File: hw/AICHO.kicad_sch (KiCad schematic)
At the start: 31 parts, among them J1 Conn_01x06, J2 Conn_01x02, J3 USB_A, U1 RP2040, U2 W25Q128JVPIQ, U3 SPX3819M5-L-3-3, Y1 12MHz

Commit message: Finish board schematic
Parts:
- added C18: 10u, Capacitor_SMD:C_0603_1608Metric, symbol Device:C
- added C19: 100n, Capacitor_SMD:C_0603_1608Metric, symbol Device:C
- added J101, J201, J301, J401: Conn_01x03, Connector_PinHeader_2.54mm:PinHeader_1x03_P2.54mm_Vertical, symbol Connector_Generic:Conn_01x03
- added J102, J103, J104, J202, J203, J204, J302, J303, J304, J402, J403, J404: Conn_01x02, Connector_PinHeader_2.54mm:PinHeader_1x02_P2.54mm_Vertical, symbol Connector_Generic:Conn_01x02
- added J4: AudioJack3_SwitchTR, Connector_Audio:Jack_3.5mm_CUI_SJ1-3525N_Horizontal, symbol Connector_Audio:AudioJack3_SwitchTR
- added J5: Speaker, Connector_PinHeader_2.54mm:PinHeader_1x02_P2.54mm_Vertical, symbol Device:Speaker
- added Q1, Q10, Q11, Q12, Q2, Q3, Q4, Q5, Q6, Q7, Q8, Q9: Si2302, Package_TO_SOT_SMD:SOT-23, symbol Device:Q_NMOS_GSD
- added U4: USBLC6-2SC6, Package_TO_SOT_SMD:SOT-23-6, symbol Power_Protection:USBLC6-2SC6
- added U5: MAX98357AETE+, MAX98357AETE+:QFN50P300X300X80-17N, symbol MAX98357AETE+:MAX98357AETE+
- C1, C10, C11, C12, C13, C14, C15, C2, C3, C4, C5, C6, C7, C8, C9: footprint (none) -> Capacitor_SMD:C_0603_1608Metric
- J1: footprint (none) -> AICHO_footprints:TestPoints_1x06_P2.0
- J2: footprint (none) -> Connector_PinHeader_2.54mm:PinHeader_1x02_P2.54mm_Vertical
- J3: footprint (none) -> Connector_USB:USB_A_CNCTech_1001-011-01101_Horizontal
- JP1: footprint (none) -> Jumper:SolderJumper-2_P1.3mm_Open_RoundedPad1.0x1.5mm
- L1: footprint (none) -> Inductor_SMD:L_0805_2012Metric
- R1, R2, R3, R4, R5: footprint (none) -> Resistor_SMD:R_0603_1608Metric
- Y1: footprint (none) -> Crystal:Crystal_SMD_3225-4Pin_3.2x2.5mm
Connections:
- net +5V: now also C18.1, C19.1, J101.1 (Pin_1), J102.1 (Pin_1), J103.1 (Pin_1), J104.1 (Pin_1), J201.1 (Pin_1), J202.1 (Pin_1), J203.1 (Pin_1), J204.1 (Pin_1), J301.1 (Pin_1), J302.1 (Pin_1), J303.1 (Pin_1), J304.1 (Pin_1), J401.1 (Pin_1), J402.1 (Pin_1), J403.1 (Pin_1), J404.1 (Pin_1), U4.5 (VBUS), U5.4 (~{SD_MODE}), U5.7 (VDD_1), U5.8 (VDD_2)
- net GND: now also J101.3 (Pin_3), J201.3 (Pin_3), J301.3 (Pin_3), J401.3 (Pin_3), Q1.2 (S), Q10.2 (S), Q11.2 (S), Q12.2 (S), Q2.2 (S), Q3.2 (S), Q4.2 (S), Q5.2 (S), Q6.2 (S), Q7.2 (S), Q8.2 (S), Q9.2 (S), U4.2 (GND), U5.11 (GND_2), U5.15 (GND_3), U5.17 (GND_4), U5.3 (GND_1)
- net USB_D+: now also U4.1 (I/O1); no longer J3.3 (D+)
- net USB_D-: now also U4.3 (I/O2); no longer J3.2 (D-)
- net ORG1_LED: now reaches U1.11 (GPIO8)
- net ORG1_LED: now also J101.2 (Pin_2)
- net ORG1_SOLENOID: now reaches U1.12 (GPIO9)
- net ORG1_SOLENOID: now also Q1.1 (G)
- net ORG1_PUMP_INFLATE: now reaches U1.13 (GPIO10)
- net ORG1_PUMP_INFLATE: now also Q2.1 (G)
- net ORG1_PUMP_DRAIN: now reaches U1.14 (GPIO11)
- net ORG1_PUMP_DRAIN: now also Q3.1 (G)
- net ORG2_LED: now reaches U1.15 (GPIO12)
- net ORG2_LED: now also J201.2 (Pin_2)
- net ORG2_SOLENOID: now reaches U1.16 (GPIO13)
- net ORG2_SOLENOID: now also Q4.1 (G)
- net ORG2_PUMP_INFLATE: now reaches U1.17 (GPIO14)
- net ORG2_PUMP_INFLATE: now also Q5.1 (G)
- net ORG2_PUMP_DRAIN: now reaches U1.18 (GPIO15)
- net ORG2_PUMP_DRAIN: now also Q6.1 (G)
- net ORG3_LED: now reaches U1.29 (GPIO18)
- net ORG3_LED: now also J301.2 (Pin_2)
- net ORG3_SOLENOID: now reaches U1.30 (GPIO19)
- net ORG3_SOLENOID: now also Q7.1 (G)
- net ORG3_PUMP_INFLATE: now reaches U1.31 (GPIO20)
- net ORG3_PUMP_INFLATE: now also Q8.1 (G)
- net ORG3_PUMP_DRAIN: now reaches U1.32 (GPIO21)
- net ORG3_PUMP_DRAIN: now also Q9.1 (G)
- net ORG4_LED: now reaches U1.34 (GPIO22)
- net ORG4_LED: now also J401.2 (Pin_2)
- net ORG4_SOLENOID: now reaches U1.35 (GPIO23)
- net ORG4_SOLENOID: now also Q10.1 (G)
- net ORG4_PUMP_INFLATE: now reaches U1.36 (GPIO24)
- net ORG4_PUMP_INFLATE: now also Q11.1 (G)
- net ORG4_PUMP_DRAIN: now reaches U1.37 (GPIO25)
- net ORG4_PUMP_DRAIN: now also Q12.1 (G)
- net I2S_CK: now reaches U1.4 (GPIO2)
- net I2S_CK: now also U5.16 (BCLK)
- net I2S_WS: now reaches U1.5 (GPIO3)
- net I2S_WS: now also U5.14 (LRCLK)
- net I2S_SD: now reaches U1.6 (GPIO4)
- net I2S_SD: now also U5.1 (DIN)
- new net: J303.2 (Pin_2), Q8.3 (D)
- new net: J404.2 (Pin_2), Q12.3 (D)
- new net: J403.2 (Pin_2), Q11.3 (D)
- new net: J402.2 (Pin_2), Q10.3 (D)
- new net: J104.2 (Pin_2), Q3.3 (D)
- new net: J302.2 (Pin_2), Q7.3 (D)
- new net: J304.2 (Pin_2), Q9.3 (D)
- new net: J103.2 (Pin_2), Q2.3 (D)
- new net: J202.2 (Pin_2), Q4.3 (D)
- new net: J204.2 (Pin_2), Q6.3 (D)
- new net: C18.2, C19.2
- new net: J102.2 (Pin_2), Q1.3 (D)
- new net: J203.2 (Pin_2), Q5.3 (D)
- new net AUDIO_OUT+: J4.R, J4.T, U5.9 (OUTP)
- new net AUDIO_OUT-: J4.S, J5.2, U5.10 (OUTN)
- new net AUDIO_SPEAKER+: J4.RN, J5.1
- new net USB_RAW_D+: J3.3 (D+), U4.6 (I/O1)
- new net USB_RAW_D-: J3.2 (D-), U4.4 (I/O2)
- no-connect marks 0 -> 15
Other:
- note added: "+9 dB gain"
- note added: "Audio Output"
- note added: "Debug"
- note added: "MCU"
- note added: "Not shut down Selected channel: L"
- note added: "Physical Output"
- note added: "Power"
- note added: "USB"
- moved on the sheet: C15, J1, J3, L1, U2

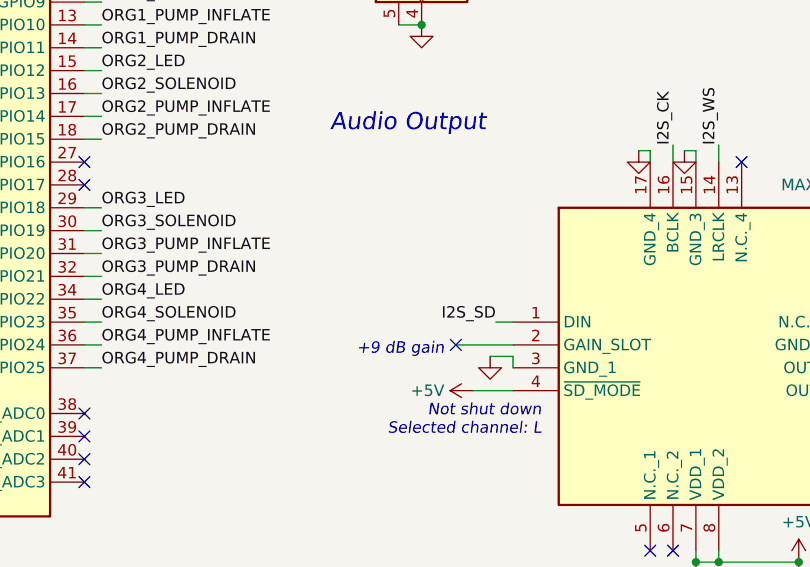
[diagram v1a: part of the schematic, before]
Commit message: Set amplifier IC to minimum gain
Ref. https://ez.analog.com/audio/f/q-a/569114/max98357-headphone-circuit
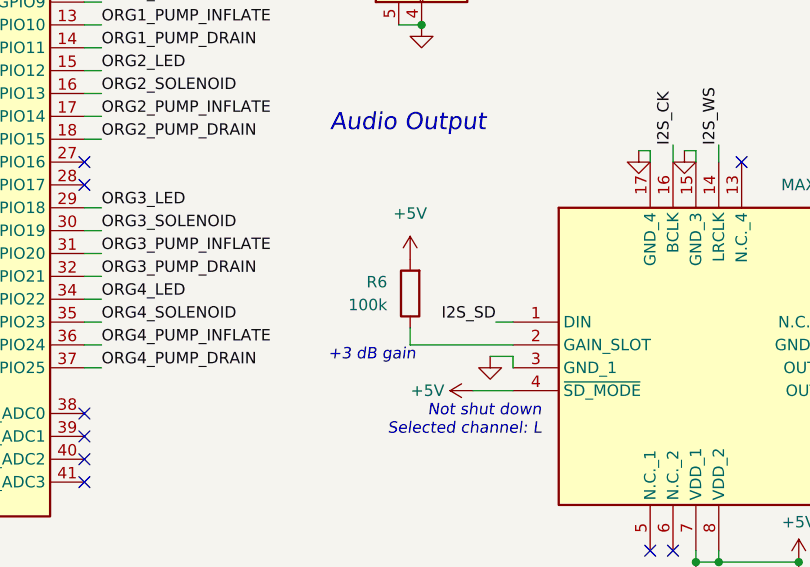
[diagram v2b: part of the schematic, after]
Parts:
- added R6: 100k, Resistor_SMD:R_0603_1608Metric, symbol Device:R
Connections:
- net +5V: now also R6.2
- net at U5.2 (GAIN_SLOT): now also R6.1
- no-connect marks 15 -> 14
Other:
- note added: "+3 dB gain"
- note removed: "+9 dB gain"
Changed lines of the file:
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@@
   (no_connect (at 219.075 121.92))
   (no_connect (at 156.21 106.68))
-  (no_connect (at 197.485 99.06))
   (no_connect (at 156.21 81.28))
   (wire (pts (xy 101.6 180.975) (xy 102.87 180.975))
@@
     (stroke (width 0) (type default))
   )
+  (wire (pts (xy 192.405 97.155) (xy 192.405 99.06))
+    (stroke (width 0) (type default))
+  )
   (wire (pts (xy 34.29 92.075) (xy 29.21 92.075))
     (stroke (width 0) (type default))
@@
     (stroke (width 0) (type default))
   )
-  (wire (pts (xy 197.485 99.06) (xy 203.835 99.06))
+  (wire (pts (xy 192.405 99.06) (xy 203.835 99.06))
     (stroke (width 0) (type default))
   )
@@
     (effects (font (size 1.27 1.27) italic) (justify right bottom))
   )
-  (text "+9 dB gain" (at 196.215 100.33 0)
+  (text "+3 dB gain" (at 193.04 100.965 0)
     (effects (font (size 1.27 1.27) italic) (justify right bottom))
   )
@@
     )
   )
+  (symbol (lib_id "power:+5V") (at 192.405 89.535 0) (unit 1)
+    (in_bom yes) (on_board yes) (dnp no) (fields_autoplaced)
+    (property "Reference" "#PWR032" (at 192.405 93.345 0)
+      (effects (font (size 1.27 1.27)) hide)
+    )
+    (property "Value" "+5V" (at 192.405 84.455 0)
+      (effects (font (size 1.27 1.27)))
+    )
+    (property "Footprint" "" (at 192.405 89.535 0)
+      (effects (font (size 1.27 1.27)) hide)
+    )
+    (property "Datasheet" "" (at 192.405 89.535 0)
+      (effects (font (size 1.27 1.27)) hide)
+    )
+    (pin "1")
+    (instances
+      (project "AICHO"
+        (path "/1352642d-7cf1-4ee5-b8a3-66f2011ace6c"
+          (reference "#PWR032") (unit 1)
+        )
+      )
+    )
+  )
   (symbol (lib_id "Connector:USB_A") (at 193.675 53.34 0) (unit 1)
     (in_bom yes) (on_board yes) (dnp no) (fields_autoplaced)
@@
         )
       )
+    )
+  )
+  (symbol (lib_id "Device:R") (at 192.405 93.345 180) (unit 1)
+    (in_bom yes) (on_board yes) (dnp no)
+    (property "Reference" "R6" (at 189.865 92.075 0)
+      (effects (font (size 1.27 1.27)) (justify left))
+    )
+    (property "Value" "100k" (at 189.865 94.615 0)
+      (effects (font (size 1.27 1.27)) (justify left))
+    )
+    (property "Footprint" "Resistor_SMD:R_0603_1608Metric" (at 194.183 93.345 90)
+      (effects (font (size 1.27 1.27)) hide)
+    )
+    (property "Datasheet" "~" (at 192.405 93.345 0)
+      (effects (font (size 1.27 1.27)) hide)
+    )
+    (pin "2")
+    (pin "1")
+    (instances
+      (project "AICHO"
+        (path "/1352642d-7cf1-4ee5-b8a3-66f2011ace6c"
+          (reference "R6") (unit 1)
+        )
+      )

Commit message: 🚧 Layout
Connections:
- net I2S_CK: now also U1.29 (GPIO18); no longer U1.4 (GPIO2)
- net I2S_SD: now also U1.31 (GPIO20); no longer U1.6 (GPIO4)
- net I2S_WS: now also U1.30 (GPIO19); no longer U1.5 (GPIO3)
- net ORG1_LED: now also U1.41 (GPIO29_ADC3); no longer U1.11 (GPIO8)
- net ORG1_PUMP_DRAIN: now also U1.5 (GPIO3); no longer U1.14 (GPIO11)
- net ORG1_PUMP_INFLATE: now also U1.4 (GPIO2); no longer U1.13 (GPIO10)
- net ORG1_SOLENOID: now also U1.3 (GPIO1); no longer U1.12 (GPIO9)
- net ORG2_LED: now also U1.40 (GPIO28_ADC2); no longer U1.15 (GPIO12)
- net ORG2_PUMP_DRAIN: now also U1.9 (GPIO7); no longer U1.18 (GPIO15)
- net ORG2_PUMP_INFLATE: now also U1.8 (GPIO6); no longer U1.17 (GPIO14)
- net ORG2_SOLENOID: now also U1.7 (GPIO5); no longer U1.16 (GPIO13)
- net ORG3_LED: now also U1.39 (GPIO27_ADC1); no longer U1.29 (GPIO18)
- net ORG3_PUMP_DRAIN: now also U1.14 (GPIO11); no longer U1.32 (GPIO21)
- net ORG3_PUMP_INFLATE: now also U1.13 (GPIO10); no longer U1.31 (GPIO20)
- net ORG3_SOLENOID: now also U1.12 (GPIO9); no longer U1.30 (GPIO19)
- net ORG4_LED: now also U1.38 (GPIO26_ADC0); no longer U1.34 (GPIO22)
- net ORG4_PUMP_DRAIN: now also U1.18 (GPIO15); no longer U1.37 (GPIO25)
- net ORG4_PUMP_INFLATE: now also U1.17 (GPIO14); no longer U1.36 (GPIO24)
- net ORG4_SOLENOID: now also U1.16 (GPIO13); no longer U1.35 (GPIO23)
- net UART_RX: now also U1.28 (GPIO17); no longer U1.3 (GPIO1)
- net UART_TX: now also U1.27 (GPIO16); no longer U1.2 (GPIO0)
- net USB_D+: now also U4.3 (I/O2); no longer U4.1 (I/O1)
- net USB_D-: now also U4.1 (I/O1); no longer U4.3 (I/O2)
- net USB_RAW_D+: now also U4.4 (I/O2); no longer U4.6 (I/O1)
- net USB_RAW_D-: now also U4.6 (I/O1); no longer U4.4 (I/O2)
- no-connect marks 14 -> 10

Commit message: 🚧 More layout
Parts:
- removed C8: 100n, Capacitor_SMD:C_0603_1608Metric, symbol Device:C
- added D1, D2: Pink, LED_SMD:LED_0603_1608Metric, symbol Device:LED
- added R7, R8: 7.5k, Resistor_SMD:R_0603_1608Metric, symbol Device:R
- C1, C2, C3, C4, C5, C6, C7: footprint Capacitor_SMD:C_0603_1608Metric -> Capacitor_SMD:C_0402_1005Metric
- C10: renamed from C11; footprint Capacitor_SMD:C_0603_1608Metric -> Capacitor_SMD:C_0402_1005Metric
- C11: renamed from C12; footprint Capacitor_SMD:C_0603_1608Metric -> Capacitor_SMD:C_0402_1005Metric
- C12: renamed from C13; footprint Capacitor_SMD:C_0603_1608Metric -> Capacitor_SMD:C_0402_1005Metric
- C13: renamed from C14; footprint Capacitor_SMD:C_0603_1608Metric -> Capacitor_SMD:C_0402_1005Metric
- C14: renamed from C15; footprint Capacitor_SMD:C_0603_1608Metric -> Capacitor_SMD:C_0402_1005Metric
- C18: renamed from C19; footprint Capacitor_SMD:C_0603_1608Metric -> Capacitor_SMD:C_0402_1005Metric
- C8: renamed from C9; footprint Capacitor_SMD:C_0603_1608Metric -> Capacitor_SMD:C_0402_1005Metric
- C9: renamed from C10; footprint Capacitor_SMD:C_0603_1608Metric -> Capacitor_SMD:C_0402_1005Metric
- renumbered C16 to C15, C17 to C16, C18 to C17
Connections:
- net GND: now also R7.2, R8.2
- net ORG1_PUMP_DRAIN: now also U1.7 (GPIO5); no longer U1.5 (GPIO3)
- net ORG1_PUMP_INFLATE: now also U1.6 (GPIO4); no longer U1.4 (GPIO2)
- net ORG1_SOLENOID: now also U1.5 (GPIO3); no longer U1.3 (GPIO1)
- net ORG2_PUMP_DRAIN: now also U1.11 (GPIO8); no longer U1.9 (GPIO7)
- net ORG2_PUMP_INFLATE: now also U1.9 (GPIO7); no longer U1.8 (GPIO6)
- net ORG2_SOLENOID: now also U1.8 (GPIO6); no longer U1.7 (GPIO5)
- net ORG4_PUMP_DRAIN: now also U1.17 (GPIO14); no longer U1.18 (GPIO15)
- net ORG4_PUMP_INFLATE: now also U1.16 (GPIO13); no longer U1.17 (GPIO14)
- net ORG4_SOLENOID: now also U1.15 (GPIO12); no longer U1.16 (GPIO13)
- net USB_D+: now also U4.1 (I/O1); no longer U4.3 (I/O2)
- net USB_D-: now also U4.3 (I/O2); no longer U4.1 (I/O1)
- net USB_RAW_D+: now also U4.6 (I/O1); no longer U4.4 (I/O2)
- net USB_RAW_D-: now also U4.4 (I/O2); no longer U4.6 (I/O1)
- net at C12.2, U1.20 (XIN): now also Y1.3; no longer Y1.1
- net ACT1: now reaches U1.34 (GPIO22)
- net ACT1: now also D1.2 (A)
- net ACT2: now reaches U1.35 (GPIO23)
- net ACT2: now also D2.2 (A)
- net at C13.2, R1.1: now also Y1.1; no longer Y1.3
- new net: D1.1 (K), R7.1
- new net: D2.1 (K), R8.1
- no-connect marks 10 -> 12
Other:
- note added: "Activity Indicators"
- moved on the sheet: Y1

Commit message: 🚧 More layout?
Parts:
- added H1, H2, H3, H4: MountingHole_Pad, MountingHole:MountingHole_2.5mm_Pad_Via, symbol Mechanical:MountingHole_Pad
- D2: value Pink -> Violet
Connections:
- net GND: now also H1.1, H2.1, H3.1, H4.1
- net I2S_CK: now also U1.5 (GPIO3); no longer U1.29 (GPIO18)
- net I2S_SD: now also U1.4 (GPIO2); no longer U1.31 (GPIO20)
- net I2S_WS: now also U1.6 (GPIO4); no longer U1.30 (GPIO19)
- net ORG1_LED: now also U1.14 (GPIO11); no longer U1.41 (GPIO29_ADC3)
- net ORG1_PUMP_DRAIN: now also U1.9 (GPIO7); no longer U1.7 (GPIO5)
- net ORG1_PUMP_INFLATE: now also U1.8 (GPIO6); no longer U1.6 (GPIO4)
- net ORG1_SOLENOID: now also U1.7 (GPIO5); no longer U1.5 (GPIO3)
- net ORG2_LED: now also U1.15 (GPIO12); no longer U1.40 (GPIO28_ADC2)
- net ORG2_PUMP_DRAIN: now also U1.13 (GPIO10); no longer U1.11 (GPIO8)
- net ORG2_PUMP_INFLATE: now also U1.12 (GPIO9); no longer U1.9 (GPIO7)
- net ORG2_SOLENOID: now also U1.11 (GPIO8); no longer U1.8 (GPIO6)
- net ORG3_LED: now also U1.16 (GPIO13); no longer U1.39 (GPIO27_ADC1)
- net ORG3_PUMP_DRAIN: now also U1.31 (GPIO20); no longer U1.14 (GPIO11)
- net ORG3_PUMP_INFLATE: now also U1.30 (GPIO19); no longer U1.13 (GPIO10)
- net ORG3_SOLENOID: now also U1.29 (GPIO18); no longer U1.12 (GPIO9)
- net ORG4_LED: now also U1.17 (GPIO14); no longer U1.38 (GPIO26_ADC0)
- net ORG4_PUMP_DRAIN: now also U1.41 (GPIO29_ADC3); no longer U1.17 (GPIO14)
- net ORG4_PUMP_INFLATE: now also U1.40 (GPIO28_ADC2); no longer U1.16 (GPIO13)
- net ORG4_SOLENOID: now also U1.39 (GPIO27_ADC1); no longer U1.15 (GPIO12)

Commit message: Finish layout and routing
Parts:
- C12, C13: value 22p -> 27p
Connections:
- net GND: now also C17.2, C18.2
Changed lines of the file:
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@@
 (kicad_sch (version 20230121) (generator eeschema)
   (paper "A4")
+  (junction (at 235.585 130.81) (diameter 0) (color 0 0 0 0)
+  )
   (junction (at 182.245 22.225) (diameter 0) (color 0 0 0 0)
   )
@@
     )
   )
+  (symbol (lib_id "power:GND") (at 235.585 130.81 0) (unit 1)
+    (in_bom yes) (on_board yes) (dnp no) (fields_autoplaced)
+    (property "Reference" "#PWR068" (at 235.585 137.16 0)
+      (effects (font (size 1.27 1.27)) hide)
+    )
+    (property "Value" "GND" (at 235.585 135.255 0)
+      (effects (font (size 1.27 1.27)) hide)
+    )
+    (property "Footprint" "" (at 235.585 130.81 0)
+      (effects (font (size 1.27 1.27)) hide)
+    )
+    (property "Datasheet" "" (at 235.585 130.81 0)
+      (effects (font (size 1.27 1.27)) hide)
+    )
+    (pin "1")
+    (instances
+      (project "AICHO"
+        (path "/1352642d-7cf1-4ee5-b8a3-66f2011ace6c"
+          (reference "#PWR068") (unit 1)
+        )
+      )
+    )
+  )
   (symbol (lib_id "power:GND") (at 110.49 238.125 0) (unit 1)
     (in_bom yes) (on_board yes) (dnp no) (fields_autoplaced)
@@
       (effects (font (size 1.27 1.27)))
     )
-    (property "Value" "22p" (at 68.58 89.535 90)
+    (property "Value" "27p" (at 68.58 89.535 90)
       (effects (font (size 1.27 1.27)))
     )
@@
       (effects (font (size 1.27 1.27)))
     )
-    (property "Value" "22p" (at 68.58 79.375 90)
+    (property "Value" "27p" (at 68.58 79.375 90)
       (effects (font (size 1.27 1.27)))
     )
